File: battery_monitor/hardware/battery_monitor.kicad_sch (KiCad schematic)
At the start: 49 parts, among them J1 VEHICLE, J2 EXT_NTC, J3 DPDT_SENSE_POLE, U1 TPS7A1633AQDGNRQ1, U2 TLV7034QPWRQ1, U3 MDBT50Q-1MV2 (logical symbol)

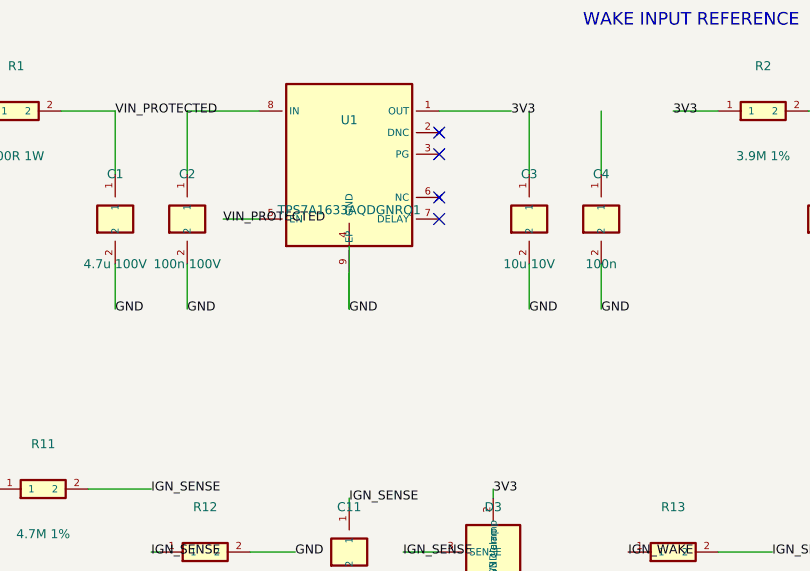
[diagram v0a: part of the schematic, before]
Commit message: Apply KiCad ERC fixes
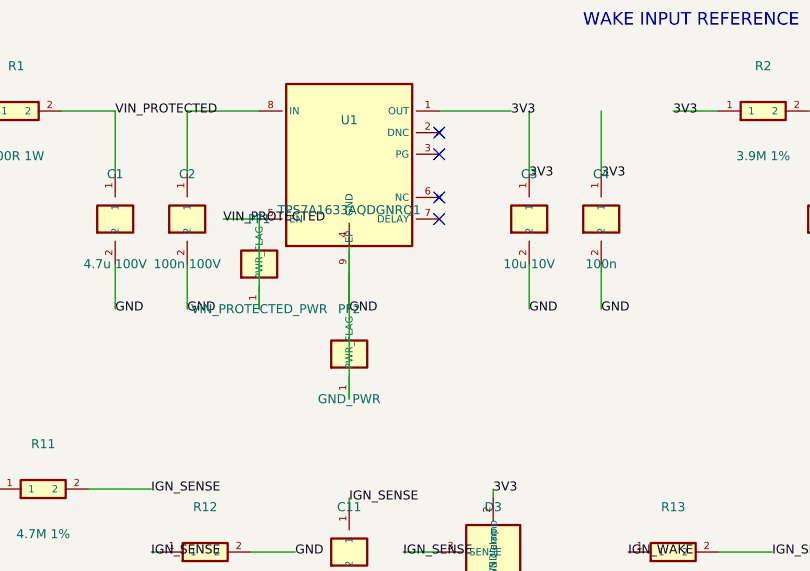
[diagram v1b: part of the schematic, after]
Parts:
- removed R13, R17, R21: 33M 1%, Resistor_SMD:R_1206_3216Metric, symbol BM:R
- added PF2: GND_PWR, symbol BM:PWRFLAG
- added R14, R18, R22: 4.7M 1%, Resistor_SMD:R_1206_3216Metric, symbol BM:R
- added R2: 3.9M 1%, Resistor_SMD:R_0805_2012Metric, symbol BM:R
- C3: renamed from C4; value 100n -> 10u 10V; footprint Capacitor_SMD:C_0805_2012Metric -> Capacitor_SMD:C_1206_3216Metric
- C4: renamed from R2; value 3.9M 1% -> 100n; footprint Resistor_SMD:R_0805_2012Metric -> Capacitor_SMD:C_0805_2012Metric; symbol BM:R -> BM:C
- PF1: renamed from C3; value 10u 10V -> VIN_PROTECTED_PWR; footprint Capacitor_SMD:C_1206_3216Metric -> (none); symbol BM:C -> BM:PWRFLAG
- R13: renamed from R14; value 4.7M 1% -> 33M 1%
- R17: renamed from R18; value 4.7M 1% -> 33M 1%
- R21: renamed from R22; value 4.7M 1% -> 33M 1%
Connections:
- net 3V3: now also C3.1, R2.1
- net DOOR_SENSE: now also R17.2
- net DOOR_WAKE: now also R17.1
- net GND: now also C4.2, PF2.1 (PWR_FLAG); no longer PF1.2
- net IGN_SENSE: now also R13.2
- net IGN_WAKE: now also R13.1
- net PARK_SENSE: now also R21.2
- net PARK_WAKE: now also R21.1
- net VEH_AUX: now also R22.1; no longer R21.1
- net VEH_DOOR: now also R14.1; no longer R13.1
- net VEH_PARK: now also R18.1; no longer R17.1
- net VIN_PROTECTED: now also PF1.1 (PWR_FLAG)
- net VREF_WAKE: now also R2.2; no longer C4.2
- net at R15.1: now also R14.2; no longer R13.2
- net at R23.1: now also R22.2; no longer R21.2
- net at R19.1: now also R18.2; no longer R17.2
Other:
- moved on the sheet: C3, C4, R13, R17, R21
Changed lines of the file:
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@@
   (wire (pts (xy 92 45) (xy 92 52)) (stroke (width 0) (type default)))
   (wire (pts (xy 92 48) (xy 92 52)) (stroke (width 0) (type default)))
+  (wire (pts (xy 82 42) (xy 82 52)) (stroke (width 0) (type default)))
+  (wire (pts (xy 92 52) (xy 92 62)) (stroke (width 0) (type default)))
   (wire (pts (xy 112 37) (xy 112 30)) (stroke (width 0) (type default)))
   (wire (pts (xy 112 47) (xy 112 52)) (stroke (width 0) (type default)))
@@
   (label "3V3" (at 110 30 0) (effects (font (size 1.0 1.0))))
   (label "GND" (at 92 52 0) (effects (font (size 1.0 1.0))))
+  (label "3V3" (at 112 37 0) (effects (font (size 1.0 1.0))))
   (label "GND" (at 112 52 0) (effects (font (size 1.0 1.0))))
+  (label "3V3" (at 120 37 0) (effects (font (size 1.0 1.0))))
   (label "GND" (at 120 52 0) (effects (font (size 1.0 1.0))))
   (label "3V3" (at 128 30 0) (effects (font (size 1.0 1.0))))
@@
     (instances (project "battery_monitor" (path "/9c88e388-d519-50ad-aef0-ab628bb0a8df" (reference "U1") (unit 1))))
   )
+  (symbol (lib_id "BM:PWRFLAG") (at 82 47 0) (unit 1) (in_bom yes) (on_board yes)
+    (property "Reference" "PF1" (at 82 42 0) (effects (font (size 1.0 1.0))))
+    (property "Value" "VIN_PROTECTED_PWR" (at 82 52 0) (effects (font (size 1.0 1.0))))
+    (property "Footprint" "" (at 82 47 0) (effects (font (size 0.8 0.8)) hide))
+    (property "Datasheet" "" (at 82 47 0) (effects (font (size 0.8 0.8)) hide))
+    (property "Description" "" (at 82 47 0) (effects (font (size 0.8 0.8)) hide))
+    (pin "1")
+    (instances (project "battery_monitor" (path "/9c88e388-d519-50ad-aef0-ab628bb0a8df" (reference "PF1") (unit 1))))
+  )
+  (symbol (lib_id "BM:PWRFLAG") (at 92 57 0) (unit 1) (in_bom yes) (on_board yes)
+    (property "Reference" "PF2" (at 92 52 0) (effects (font (size 1.0 1.0))))
+    (property "Value" "GND_PWR" (at 92 62 0) (effects (font (size 1.0 1.0))))
+    (property "Footprint" "" (at 92 57 0) (effects (font (size 0.8 0.8)) hide))
+    (property "Datasheet" "" (at 92 57 0) (effects (font (size 0.8 0.8)) hide))
+    (property "Description" "" (at 92 57 0) (effects (font (size 0.8 0.8)) hide))
+    (pin "1")
+    (instances (project "battery_monitor" (path "/9c88e388-d519-50ad-aef0-ab628bb0a8df" (reference "PF2") (unit 1))))
+  )
   (symbol (lib_id "BM:C") (at 112 42 0) (unit 1) (in_bom yes) (on_board yes)
